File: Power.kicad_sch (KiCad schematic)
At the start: 82 parts, among them J11 8-pin ATX connector, Q1 MMBT2222A, U21 SiRA80DP, U22 TPS25983, U23 AP7361C-33E, U24 MP8795, U25 MIC23201YML-TR

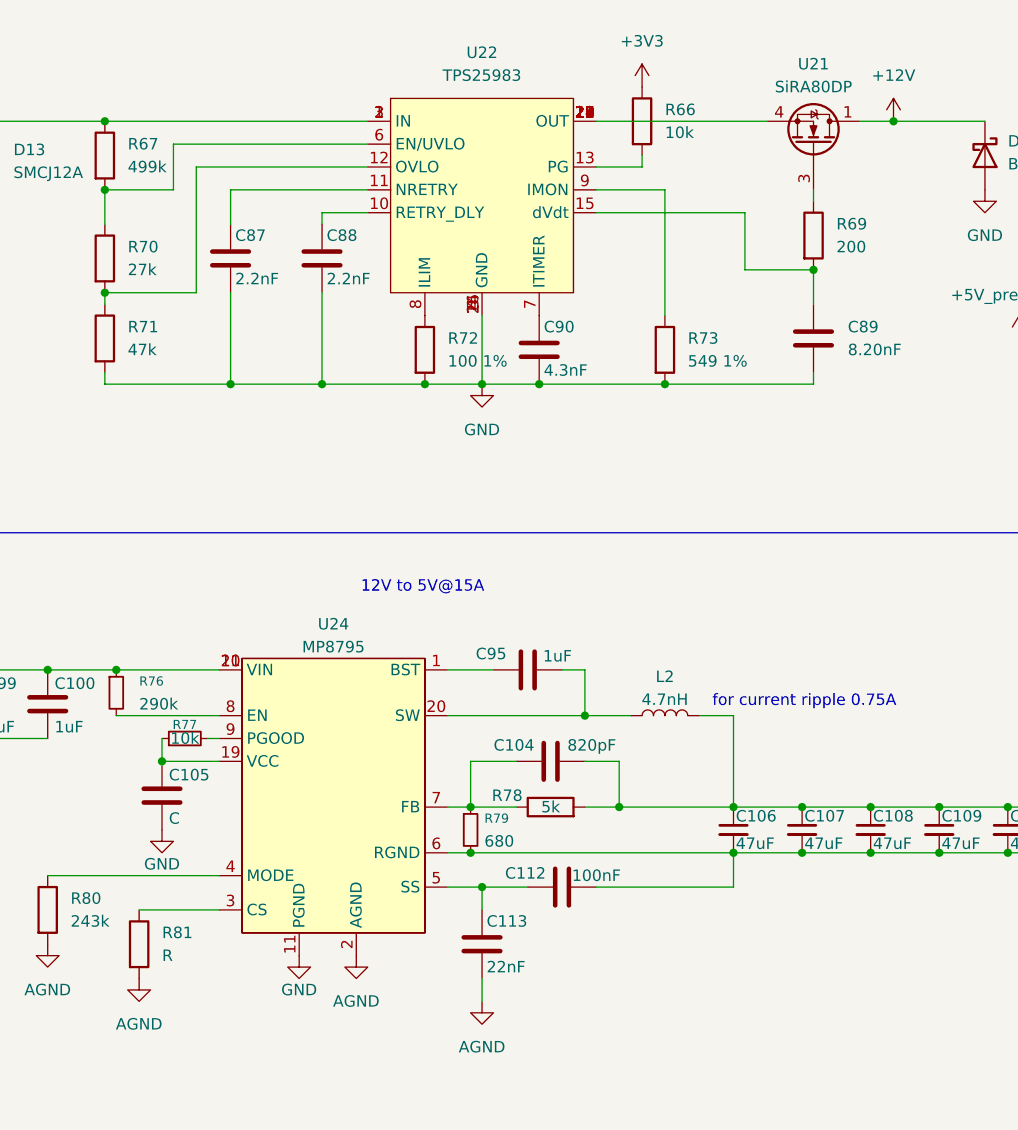
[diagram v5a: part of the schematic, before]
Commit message: Values of C105 and R81 corrected
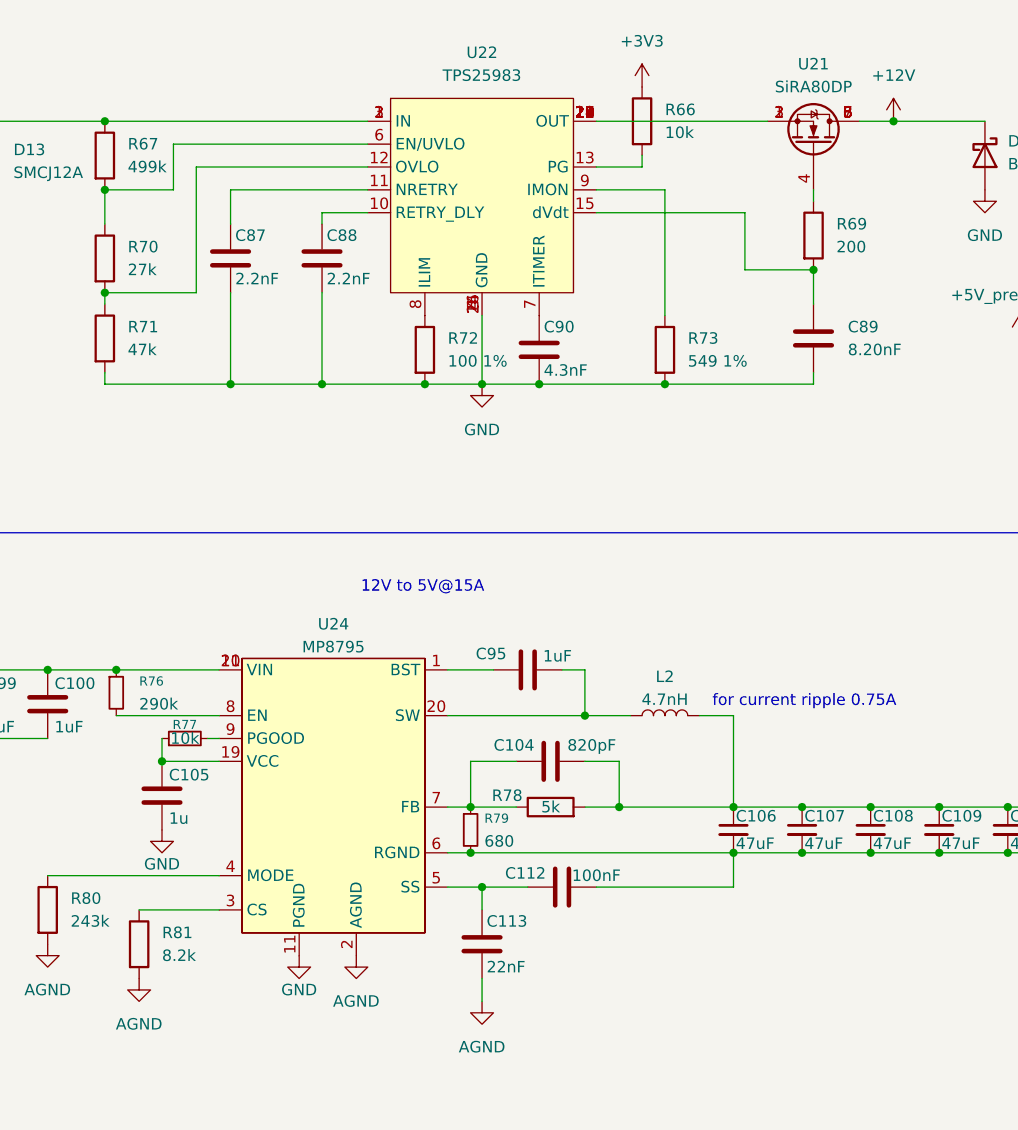
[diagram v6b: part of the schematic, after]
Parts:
- C105: value C -> 1u
- R81: value R -> 8.2k
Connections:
- net +12V: now also U21.5 (D), U21.6 (D), U21.7 (D), U21.8 (D); no longer U21.1 (D)
- net at U22.17 (OUT), U22.18 (OUT), U22.19 (OUT)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: now also U21.1 (S), U21.2 (S), U21.3 (S); no longer U21.4 (S)
- net at R69.1: now also U21.4 (G); no longer U21.3 (G)
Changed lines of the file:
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@@
 			)
 		)
-		(property "Value" "R"
+		(property "Value" "8.2k"
 			(at 62.23 120.6499 0)
 			(effects
@@
 		(pin "4"
 		)
+		(pin "7"
+		)
+		(pin "6"
+		)
+		(pin "5"
+		)
+		(pin "8"
+		)
+		(pin "2"
+		)
 		(instances
 			(project ""
@@
 			)
 		)
-		(property "Value" "C"
+		(property "Value" "1u"
 			(at 62.992 105.41 0)
 			(effects

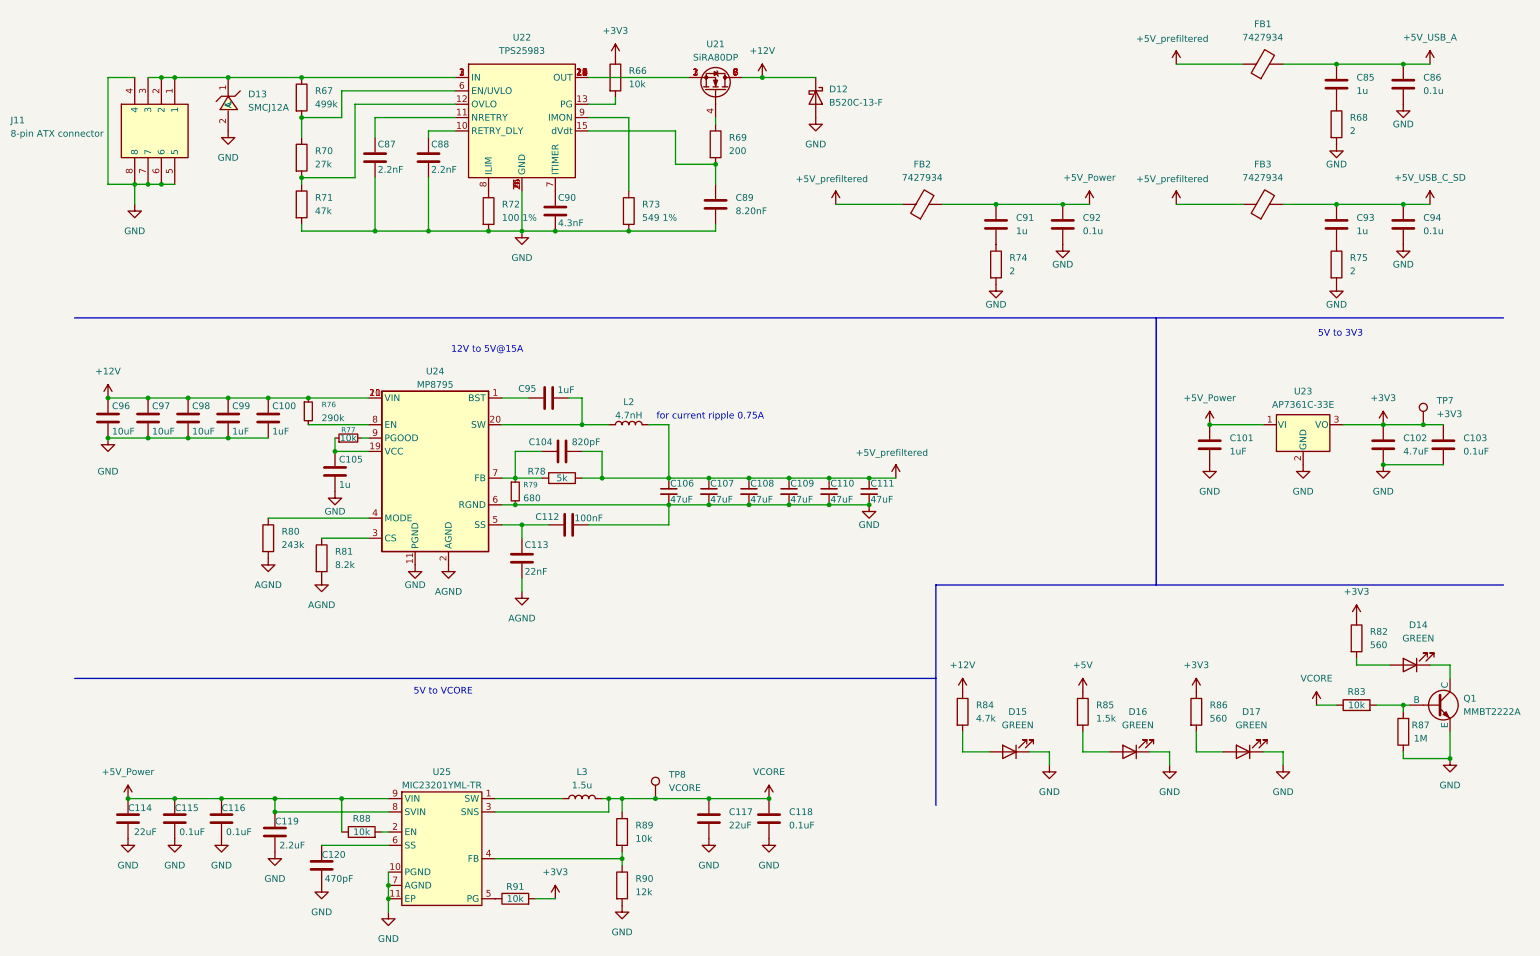
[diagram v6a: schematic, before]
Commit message: Added lcsc part number for most of components, fixes for better routing
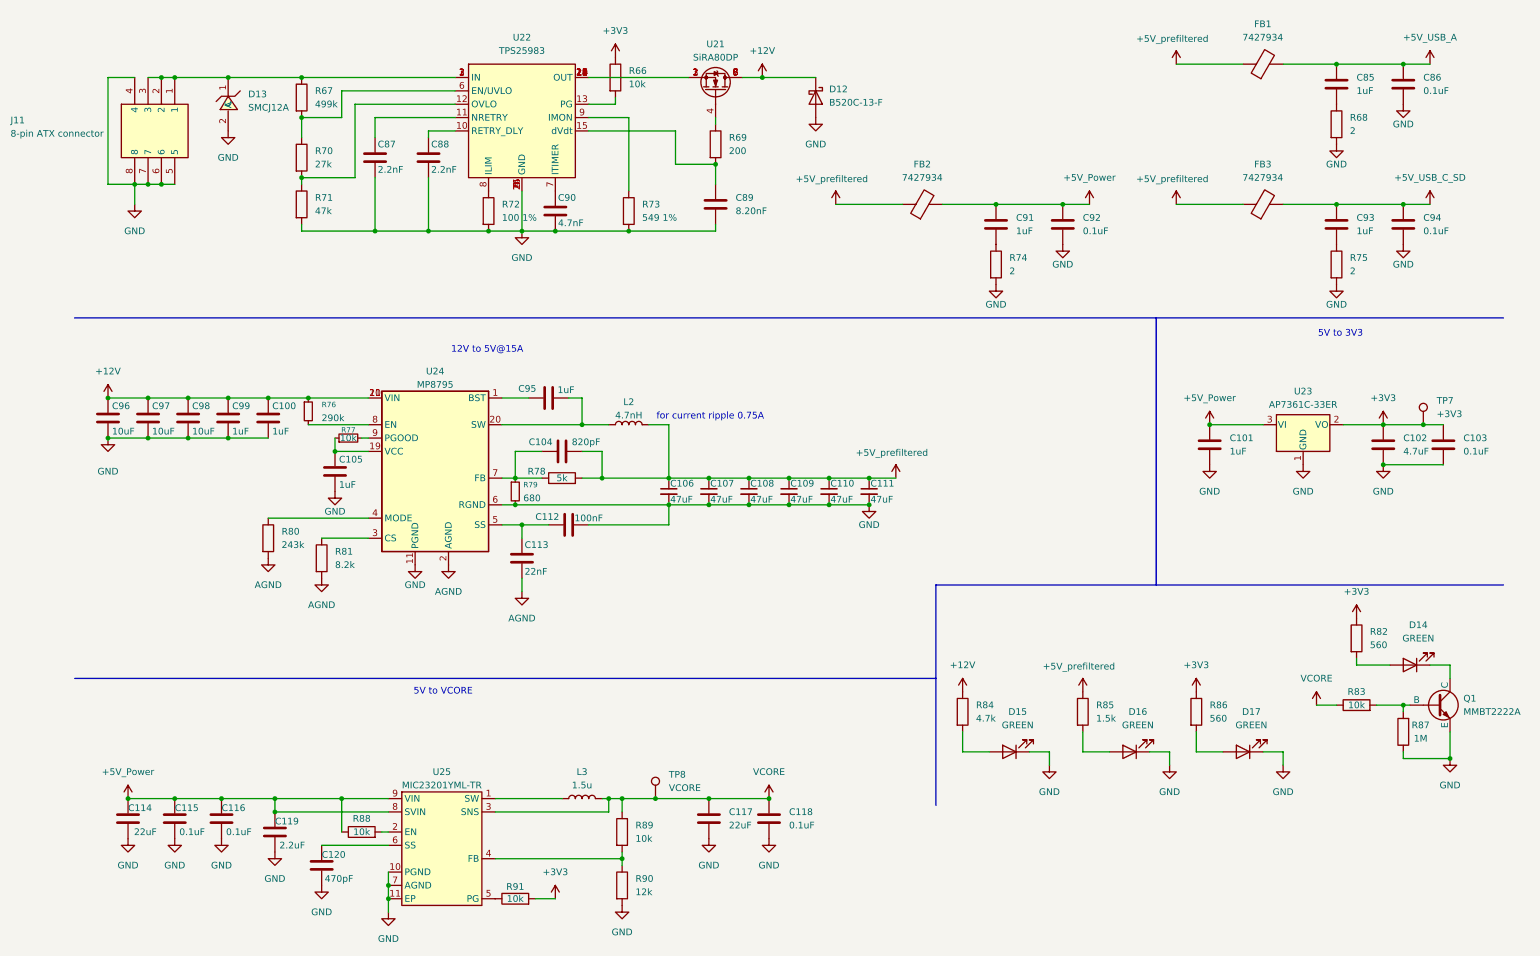
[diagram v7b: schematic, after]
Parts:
- C100, C101, C95, C99: footprint Capacitor_SMD:C_0402_1005Metric -> Capacitor_SMD:C_0603_1608Metric; LCSC Part (none) -> C5199872
- C102: footprint Capacitor_SMD:C_0402_1005Metric -> Capacitor_SMD:C_0805_2012Metric; LCSC Part (none) -> C6119944
- C103, C112, C115, C116, C118: LCSC Part (none) -> C5182432
- C104: LCSC Part (none) -> C114386
- C105, C85, C91, C93: value 1u -> 1uF; footprint Capacitor_SMD:C_0402_1005Metric -> Capacitor_SMD:C_0603_1608Metric; LCSC Part (none) -> C5199872
- C106, C107, C108, C109, C110, C111: footprint Capacitor_SMD:C_0402_1005Metric -> Capacitor_THT:C_Radial_D5.0mm_H11.0mm_P2.00mm; LCSC Part (none) -> C721300
- C113: LCSC Part (none) -> C77023
- C114, C117: footprint Capacitor_SMD:C_0402_1005Metric -> Capacitor_THT:C_Radial_D5.0mm_H11.0mm_P2.00mm; LCSC Part (none) -> C88755
- C119: LCSC Part (none) -> C2999759
- C120: LCSC Part (none) -> C272887
- C86, C92, C94: value 0.1u -> 0.1uF; LCSC Part (none) -> C5182432
- C87, C88: LCSC Part (none) -> C513667
- C89: LCSC Part (none) -> C541457
- C90: value 4.3nF -> 4.7nF; LCSC Part (none) -> C281757
- C96, C97, C98: footprint Capacitor_SMD:C_0402_1005Metric -> Capacitor_SMD:C_0805_2012Metric; LCSC Part (none) -> C3039694
- D12: LCSC Part (none) -> C134460
- D13: LCSC Part C22427765 -> C224038
- D14, D15, D16, D17: LCSC Part (none) -> C22371298
- U21: LCSC Part (none) -> C3289458
- U23: value AP7361C-33E -> AP7361C-33ER; LCSC Part (none) -> C3743528
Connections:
- net +5V is gone; now on net +5V_prefiltered: R85.1
- net +3V3: now also U23.2 (VO); no longer U23.3 (VO)
- net +5V_Power: now also U23.3 (VI); no longer U23.1 (VI)
- net GND: now also U23.1 (GND); no longer U23.2 (GND)

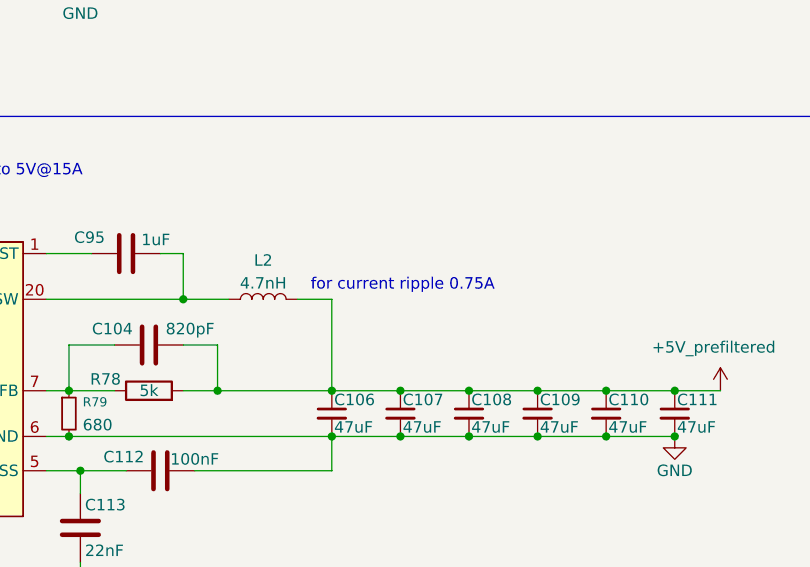
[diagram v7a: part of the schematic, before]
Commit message: Added lcsc part number for most of resistors
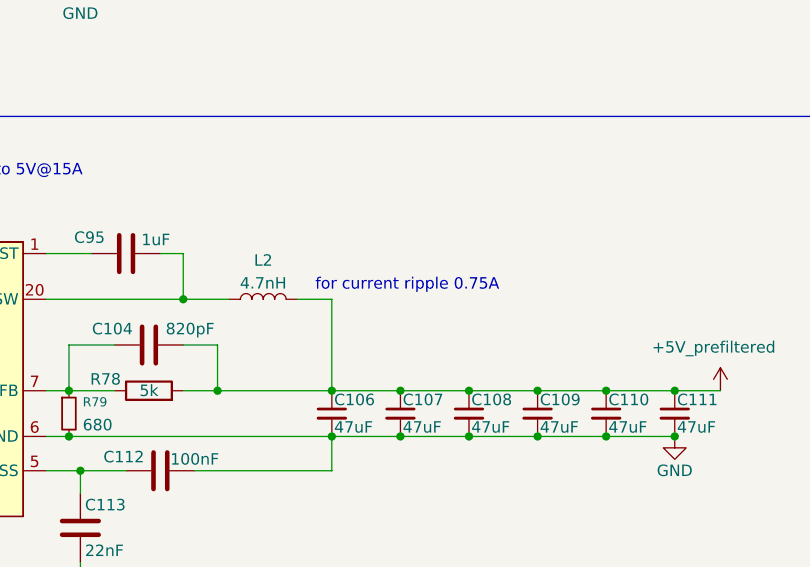
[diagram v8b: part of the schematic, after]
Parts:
- FB1, FB2, FB3: LCSC Part (none) -> C5429469
- Q1: LCSC Part (none) -> C82460
- R66, R77, R83, R88, R89, R91: LCSC Part (none) -> C25744
- R67: LCSC Part (none) -> C137971
- R68, R74, R75: footprint Resistor_SMD:R_0402_1005Metric -> Resistor_SMD:R_0603_1608Metric; LCSC Part (none) -> C2907139
- R69: LCSC Part (none) -> C114764
- R70: LCSC Part (none) -> C138022
- R71: LCSC Part (none) -> C93943
- R72: LCSC Part (none) -> C106232
- R73: LCSC Part (none) -> C7334458
- R76: LCSC Part (none) -> C5126158
- R78: LCSC Part (none) -> C5948099
- R79: LCSC Part (none) -> C25130
- R80: LCSC Part (none) -> C2998149
- R81: LCSC Part (none) -> C137929
- R82, R86: LCSC Part (none) -> C137858
- R84: LCSC Part (none) -> C105871
- R85: LCSC Part (none) -> C327253
- R87: LCSC Part (none) -> C2906900
- R90: LCSC Part (none) -> C413006
